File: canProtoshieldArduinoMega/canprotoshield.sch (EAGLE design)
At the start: 55 parts, among them CN1 1X4-3.5MM, CN10 1X4-3.5MM, CN11 1X4-3.5MM, CN12 1X4-3.5MM, CN13 1X4-3.5MM, CN14 1X4-3.5MM, CN15 1X4-3.5MM, CN16 1X4-3.5MM, CN17 1X4-3.5MM, CN18 1X4-3.5MM, CN19 1X4-3.5MM, CN2 1X4-3.5MM, CN20 1X4-3.5MM, CN21 1X4-3.5MM, CN22 1X4-3.5MM, CN23 1X4-3.5MM, CN24 1X4-3.5MM, CN25 1X4-3.5MM, CN26 1X4-3.5MM, CN27 1X4-3.5MM, CN28 1X4-3.5MM, CN29 1X4-3.5MM, CN3 1X4-3.5MM, CN30 1X4-3.5MM, CN31 1X4-3.5MM, CN32 1X4-3.5MM, CN33 1X4-3.5MM, CN34 1X4-3.5MM, CN4 1X4-3.5MM, CN5 1X4-3.5MM, CN6 1X4-3.5MM, CN7 1X4-3.5MM, CN8 1X4-3.5MM, CN9 1X4-3.5MM, Q1 16mhz, U2 MCP2551, U3 ARDUINO-MEGAFULL

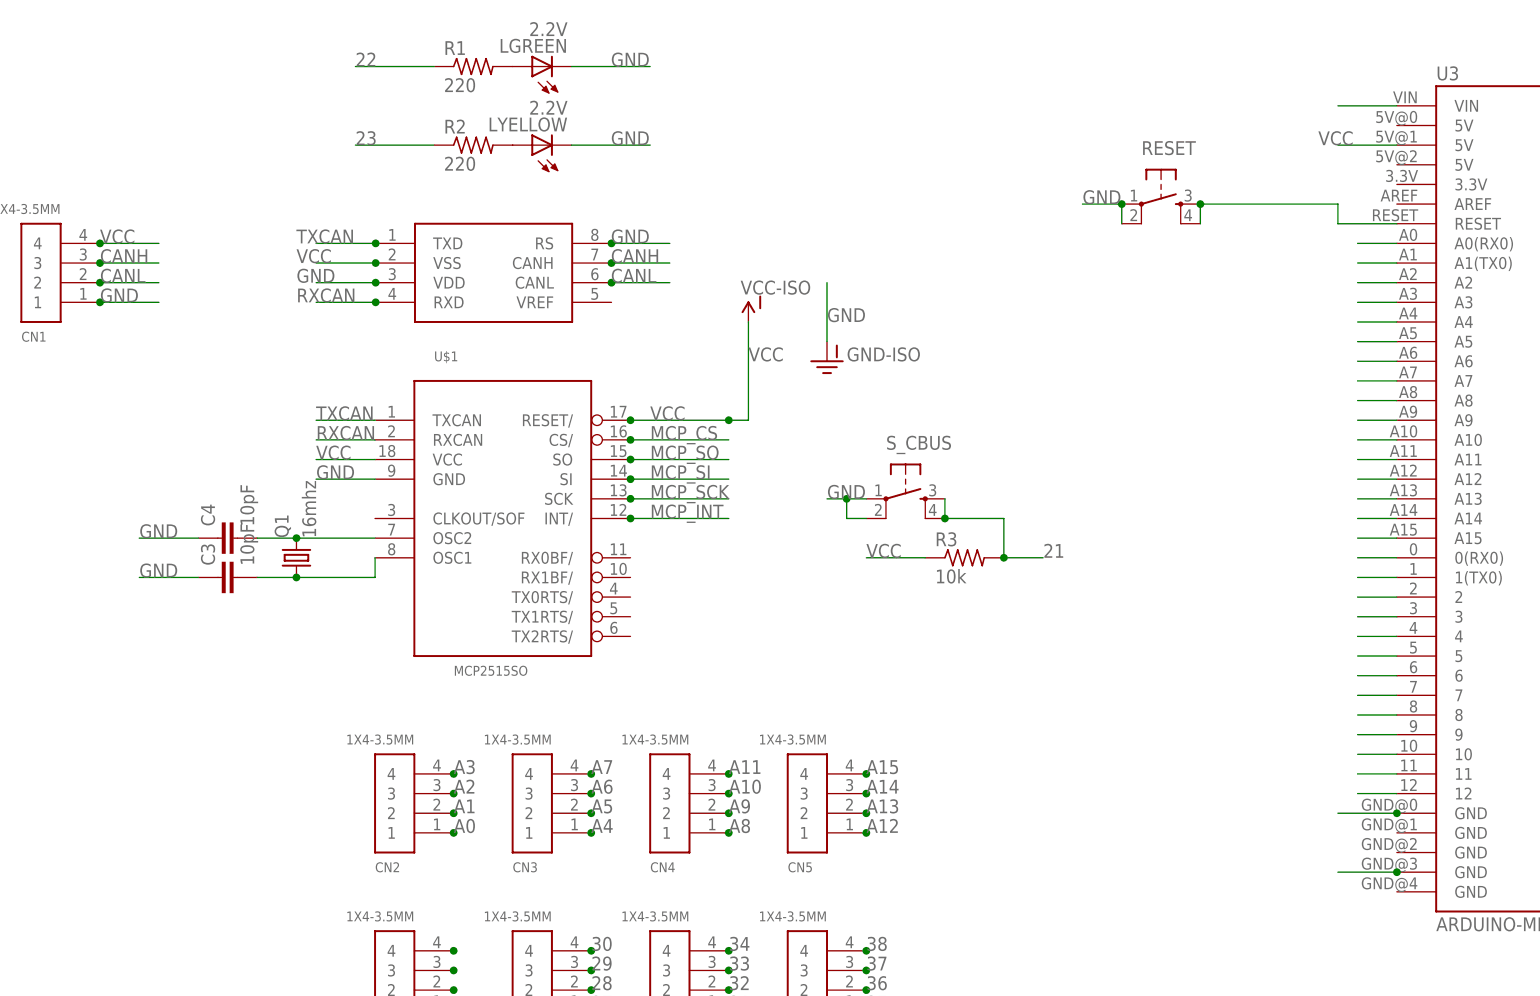
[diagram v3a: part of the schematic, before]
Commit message: Made correction on the main PCB. MCP2515 had wrong connections. Added some resistor and capacitors.
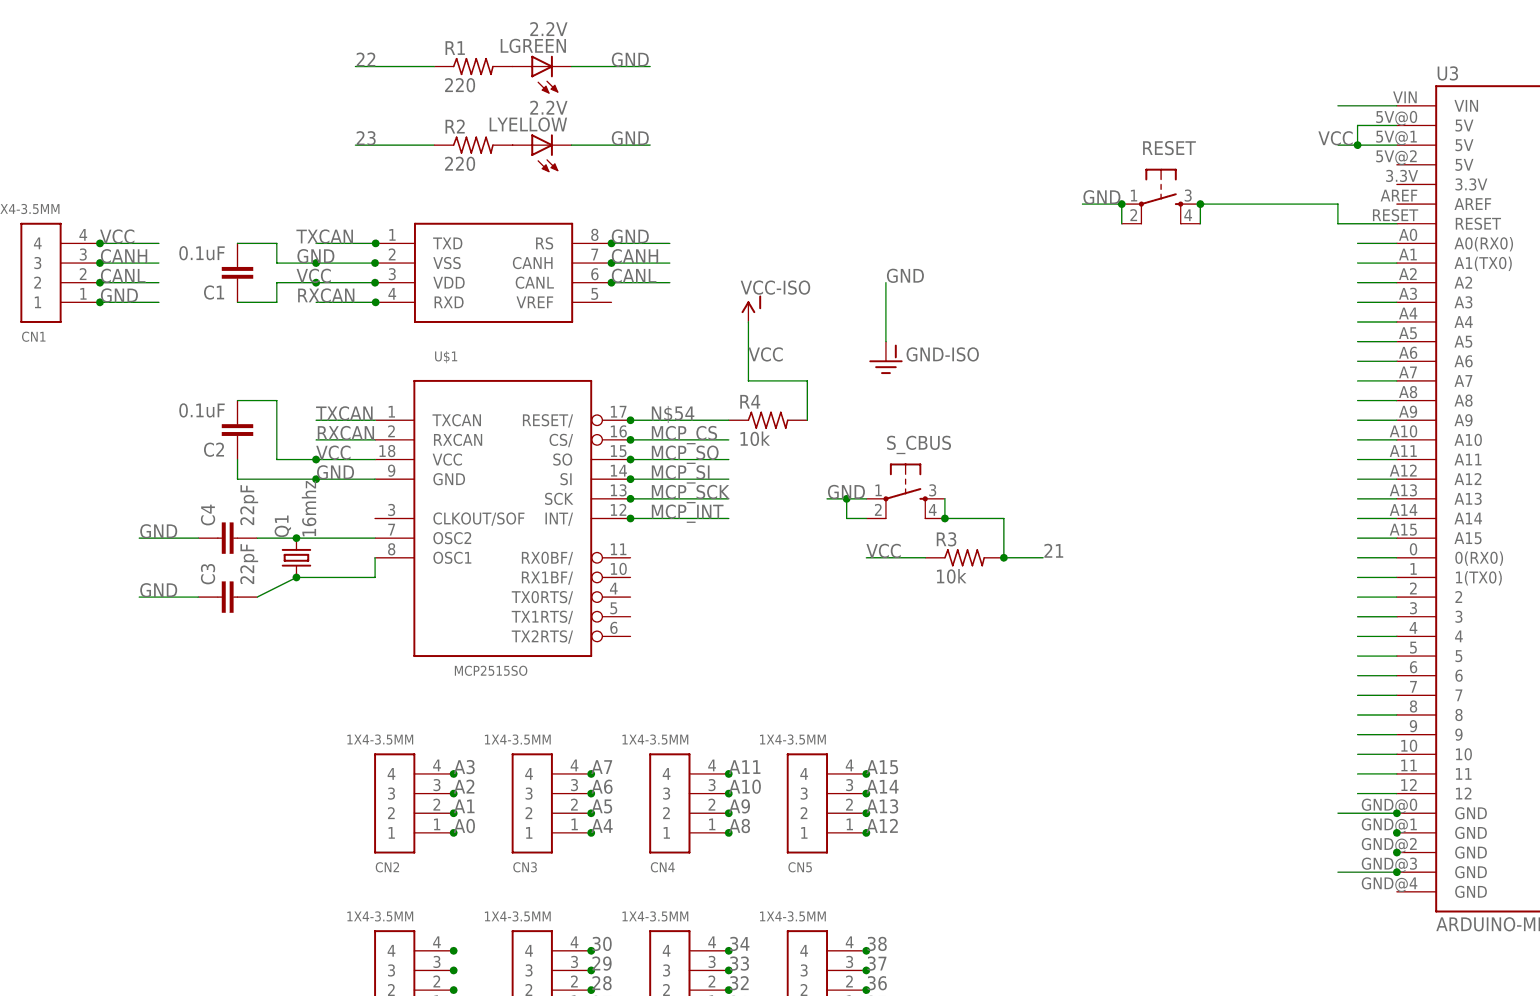
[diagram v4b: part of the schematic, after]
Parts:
- added C1, C2: 0.1uF, SparkFun-Capacitors:CAP0805
- added R4: 10k, adafruit:R-US_M2012
- C3, C4: value 10pF -> 22pF
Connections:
- new net N$54: R4.1, U$1.RESET/
- new net N$55: U3.GND@1
- new net N$56: U3.GND@2
- net GND: now also C1.2, C2.1; no longer U2.VDD
- net VCC: now also C1.1, C2.2, R4.2, U3.5V@0; no longer U$1.RESET/, U2.VSS
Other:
- moved on the sheet: C3
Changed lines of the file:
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@@
 <part name="S_CBUS" library="SparkFun-Retired" deviceset="TAC_SWITCH" device="PTH"/>
 <part name="U$1" library="MCP2515_MT" deviceset="MCP2515*" device="SO"/>
-<part name="C3" library="SparkFun-Capacitors" deviceset="CAP" device="0805" value="10pF"/>
-<part name="C4" library="SparkFun-Capacitors" deviceset="CAP" device="0805" value="10pF"/>
+<part name="C3" library="SparkFun-Capacitors" deviceset="CAP" device="0805" value="22pF"/>
+<part name="C4" library="SparkFun-Capacitors" deviceset="CAP" device="0805" value="22pF"/>
 <part name="GND" library="SparkFun-Aesthetics" deviceset="GND-ISO" device=""/>
 <part name="VCC" library="SparkFun-Aesthetics" deviceset="VCC-ISO" device=""/>
@@
 <part name="JP4" library="pinhead" deviceset="PINHD-2X24" device=""/>
 <part name="Q1" library="adafruit" deviceset="CRYSTAL" device="HC49S" value="16mhz"/>
+<part name="C1" library="SparkFun-Capacitors" deviceset="CAP" device="0805" value="0.1uF"/>
+<part name="C2" library="SparkFun-Capacitors" deviceset="CAP" device="0805" value="0.1uF"/>
+<part name="R4" library="adafruit" deviceset="R-US_" device="M2012" value="10k"/>
 </parts>
 <sheets>
@@
 <instance part="S_CBUS" gate="S" x="81.28" y="25.4"/>
 <instance part="U$1" gate="G$1" x="25.4" y="7.62"/>
-<instance part="C3" gate="G$1" x="-5.08" y="15.24" rot="R90"/>
+<instance part="C3" gate="G$1" x="-5.08" y="12.7" rot="R90"/>
 <instance part="C4" gate="G$1" x="-5.08" y="20.32" rot="R90"/>
-<instance part="GND" gate="G$1" x="71.12" y="43.18"/>
+<instance part="GND" gate="G$1" x="78.74" y="43.18"/>
 <instance part="VCC" gate="G$1" x="60.96" y="48.26"/>
 <instance part="R3" gate="G$1" x="88.9" y="17.78"/>
@@
 <instance part="JP4" gate="A" x="297.18" y="-139.7"/>
 <instance part="Q1" gate="G$1" x="2.54" y="17.78" rot="R90"/>
+<instance part="C1" gate="G$1" x="-5.08" y="55.88" rot="R180"/>
+<instance part="C2" gate="G$1" x="-5.08" y="35.56" rot="R180"/>
+<instance part="R4" gate="G$1" x="63.5" y="35.56"/>
 </instances>
 <busses>
@@
 <wire x1="12.7" y1="15.24" x2="2.54" y2="15.24" width="0.1524" layer="91"/>
 <pinref part="Q1" gate="G$1" pin="1"/>
-<wire x1="2.54" y1="15.24" x2="-2.54" y2="15.24" width="0.1524" layer="91"/>
+<wire x1="2.54" y1="15.24" x2="-2.54" y2="12.7" width="0.1524" layer="91"/>
 <junction x="2.54" y="15.24"/>
 </segment>
@@
 <segment>
 <pinref part="GND" gate="G$1" pin="GND-ISO"/>
-<wire x1="71.12" y1="45.72" x2="71.12" y2="53.34" width="0.1524" layer="91"/>
-<label x="71.12" y="48.26" size="1.778" layer="95"/>
+<wire x1="78.74" y1="45.72" x2="78.74" y2="53.34" width="0.1524" layer="91"/>
+<label x="78.74" y="53.34" size="1.778" layer="95"/>
 </segment>
 <segment>
@@
 <segment>
 <pinref part="C3" gate="G$1" pin="1"/>
-<wire x1="-10.16" y1="15.24" x2="-17.78" y2="15.24" width="0.1524" layer="91"/>
-<label x="-17.78" y="15.24" size="1.778" layer="95"/>
+<wire x1="-10.16" y1="12.7" x2="-17.78" y2="12.7" width="0.1524" layer="91"/>
+<label x="-17.78" y="12.7" size="1.778" layer="95"/>
 </segment>
 <segment>
@@
 <label x="5.08" y="27.94" size="1.778" layer="95"/>
 <pinref part="U$1" gate="G$1" pin="GND"/>
-</segment>
-<segment>
-<pinref part="U2" gate="G$1" pin="VDD"/>
-<junction x="12.78" y="53.34"/>
-<label x="2.54" y="53.34" size="1.778" layer="95"/>
-<wire x1="12.78" y1="53.34" x2="5.08" y2="53.34" width="0.1524" layer="91"/>
+<junction x="5.08" y="27.94"/>
+<pinref part="C2" gate="G$1" pin="1"/>
+<wire x1="5.08" y1="27.94" x2="-5.08" y2="27.94" width="0.1524" layer="91"/>
+<wire x1="-5.08" y1="27.94" x2="-5.08" y2="30.48" width="0.1524" layer="91"/>
 </segment>
 <segment>
@@
 <label x="269.24" y="-45.72" size="1.778" layer="95"/>
 </segment>
+<segment>
+<wire x1="12.7" y1="55.88" x2="5.08" y2="55.88" width="0.1524" layer="91"/>
+<junction x="12.7" y="55.88"/>
+<label x="2.54" y="55.88" size="1.778" layer="95"/>
+<junction x="5.08" y="55.88"/>
+<wire x1="5.08" y1="55.88" x2="0" y2="55.88" width="0.1524" layer="91"/>
+<wire x1="0" y1="55.88" x2="0" y2="58.42" width="0.1524" layer="91"/>
+<pinref part="C1" gate="G$1" pin="2"/>
+<wire x1="0" y1="58.42" x2="-5.08" y2="58.42" width="0.1524" layer="91"/>
+</segment>
 </net>
 <net name="VCC" class="0">
 <segment>
 <pinref part="VCC" gate="G$1" pin="VCC-ISO"/>
-<wire x1="60.96" y1="48.26" x2="60.96" y2="35.56" width="0.1524" layer="91"/>
+<wire x1="60.96" y1="48.26" x2="60.96" y2="40.64" width="0.1524" layer="91"/>
 <label x="60.96" y="43.18" size="1.778" layer="95"/>
-<pinref part="U$1" gate="G$1" pin="RESET/"/>
-<wire x1="45.72" y1="35.56" x2="58.42" y2="35.56" width="0.1524" layer="91"/>
-<label x="48.26" y="35.56" size="1.778" layer="95"/>
-<junction x="45.72" y="35.56"/>
-<junction x="58.42" y="35.56"/>
-<wire x1="58.42" y1="35.56" x2="60.96" y2="35.56" width="0.1524" layer="91"/>
+<pinref part="R4" gate="G$1" pin="2"/>
+<wire x1="60.96" y1="40.64" x2="68.58" y2="40.64" width="0.1524" layer="91"/>
+<wire x1="68.58" y1="40.64" x2="68.58" y2="35.56" width="0.1524" layer="91"/>
 </segment>
 <segment>
@@
 <label x="5.08" y="30.48" size="1.778" layer="95"/>
 <pinref part="U$1" gate="G$1" pin="VCC"/>
-</segment>
-<segment>
-<pinref part="U2" gate="G$1" pin="VSS"/>
-<junction x="12.78" y="55.88"/>
-<label x="2.54" y="55.88" size="1.778" layer="95"/>
-<wire x1="12.78" y1="55.88" x2="5.08" y2="55.88" width="0.1524" layer="91"/>
+<junction x="5.08" y="30.48"/>
+<wire x1="5.08" y1="30.48" x2="0" y2="30.48" width="0.1524" layer="91"/>
+<wire x1="0" y1="30.48" x2="0" y2="38.1" width="0.1524" layer="91"/>
+<pinref part="C2" gate="G$1" pin="2"/>
+<wire x1="0" y1="38.1" x2="-5.08" y2="38.1" width="0.1524" layer="91"/>
 </segment>
 <segment>
@@
 <segment>
 <pinref part="U3" gate="G$1" pin="5V@1"/>
-<wire x1="144.78" y1="71.12" x2="137.16" y2="71.12" width="0.1524" layer="91"/>
+<wire x1="144.78" y1="71.12" x2="139.7" y2="71.12" width="0.1524" layer="91"/>
 <label x="134.62" y="71.12" size="1.778" layer="95"/>
+<junction x="139.7" y="71.12"/>
+<wire x1="139.7" y1="71.12" x2="137.16" y2="71.12" width="0.1524" layer="91"/>
+<wire x1="139.7" y1="71.12" x2="139.7" y2="73.66" width="0.1524" layer="91"/>
+<pinref part="U3" gate="G$1" pin="5V@0"/>
+<wire x1="139.7" y1="73.66" x2="144.78" y2="73.66" width="0.1524" layer="91"/>
 </segment>
 <segment>
@@
 <wire x1="256.54" y1="-45.72" x2="248.92" y2="-45.72" width="0.1524" layer="91"/>
 <label x="248.92" y="-45.72" size="1.778" layer="95"/>
+</segment>
+<segment>
+<wire x1="12.7" y1="53.34" x2="5.08" y2="53.34" width="0.1524" layer="91"/>
+<junction x="12.7" y="53.34"/>
+<label x="2.54" y="53.34" size="1.778" layer="95"/>
+<junction x="5.08" y="53.34"/>
+<wire x1="5.08" y1="53.34" x2="0" y2="53.34" width="0.1524" layer="91"/>
+<wire x1="0" y1="53.34" x2="0" y2="50.8" width="0.1524" layer="91"/>
+<pinref part="C1" gate="G$1" pin="1"/>
+<wire x1="0" y1="50.8" x2="-5.08" y2="50.8" width="0.1524" layer="91"/>
 </segment>
 </net>
@@
 </segment>
 </net>
+<net name="N$54" class="0">
+<segment>
+<pinref part="U$1" gate="G$1" pin="RESET/"/>
+<wire x1="45.72" y1="35.56" x2="58.42" y2="35.56" width="0.1524" layer="91"/>
+<junction x="45.72" y="35.56"/>
+<label x="48.26" y="35.56" size="1.778" layer="95"/>
+<pinref part="R4" gate="G$1" pin="1"/>
+</segment>
+</net>
+<net name="N$55" class="0">
+<segment>
+<pinref part="U3" gate="G$1" pin="GND@1"/>
+<junction x="144.78" y="-17.78"/>
+</segment>
+</net>
+<net name="N$56" class="0">
+<segment>
+<pinref part="U3" gate="G$1" pin="GND@2"/>
+<junction x="144.78" y="-20.32"/>
+</segment>
+</net>

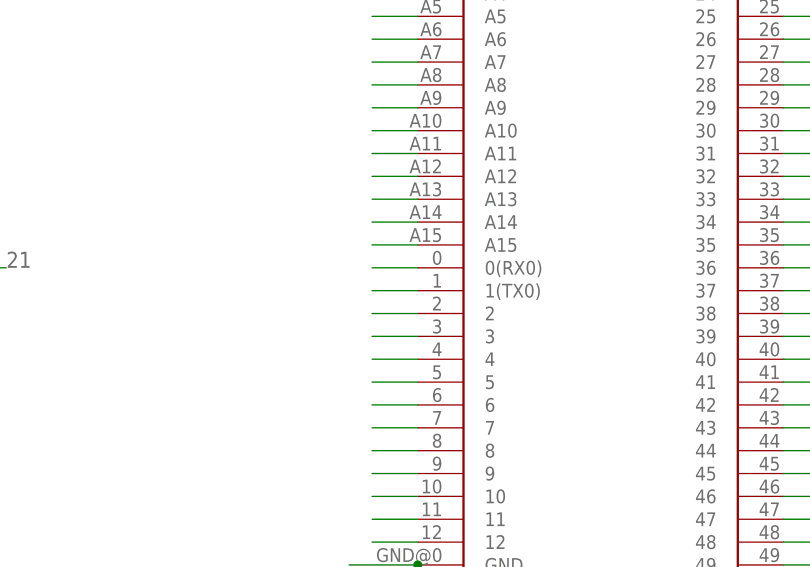
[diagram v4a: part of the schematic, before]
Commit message: Ethernet connector-previous version
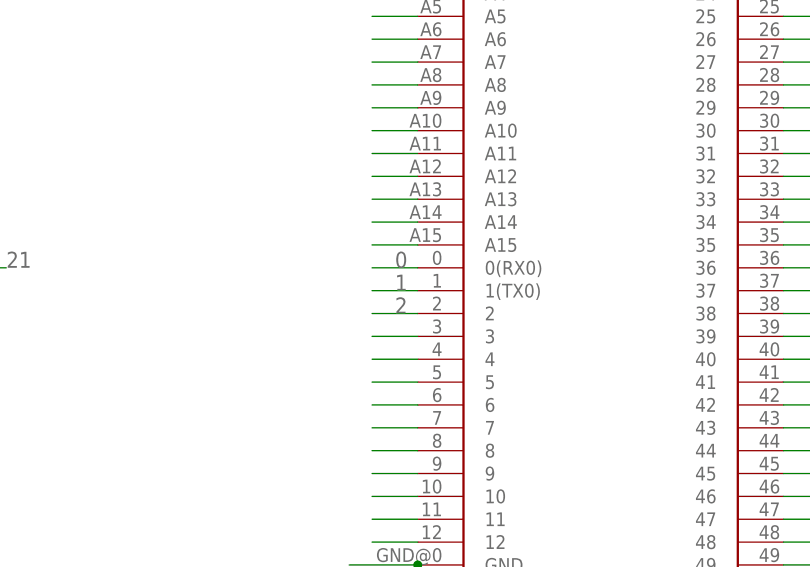
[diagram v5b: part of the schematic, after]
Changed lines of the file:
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@@
 <pinref part="U3" gate="G$1" pin="0(RX0)"/>
 <wire x1="144.78" y1="17.78" x2="139.7" y2="17.78" width="0.1524" layer="91"/>
+<label x="142.24" y="17.78" size="1.778" layer="95"/>
 </segment>
 <segment>
@@
 <pinref part="U3" gate="G$1" pin="1(TX0)"/>
 <wire x1="144.78" y1="15.24" x2="139.7" y2="15.24" width="0.1524" layer="91"/>
+<label x="142.24" y="15.24" size="1.778" layer="95"/>
 </segment>
 <segment>
@@
 <pinref part="U3" gate="G$1" pin="2"/>
 <wire x1="144.78" y1="12.7" x2="139.7" y2="12.7" width="0.1524" layer="91"/>
-</segment>
-</net>
+<label x="142.24" y="12.7" size="1.778" layer="95"/>
+</segment>
+</net>
